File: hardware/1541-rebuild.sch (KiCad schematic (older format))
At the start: 9 parts, among them IC1 ATMEGA1284P-P, P1 CONN_01X02, X1 20Mhz

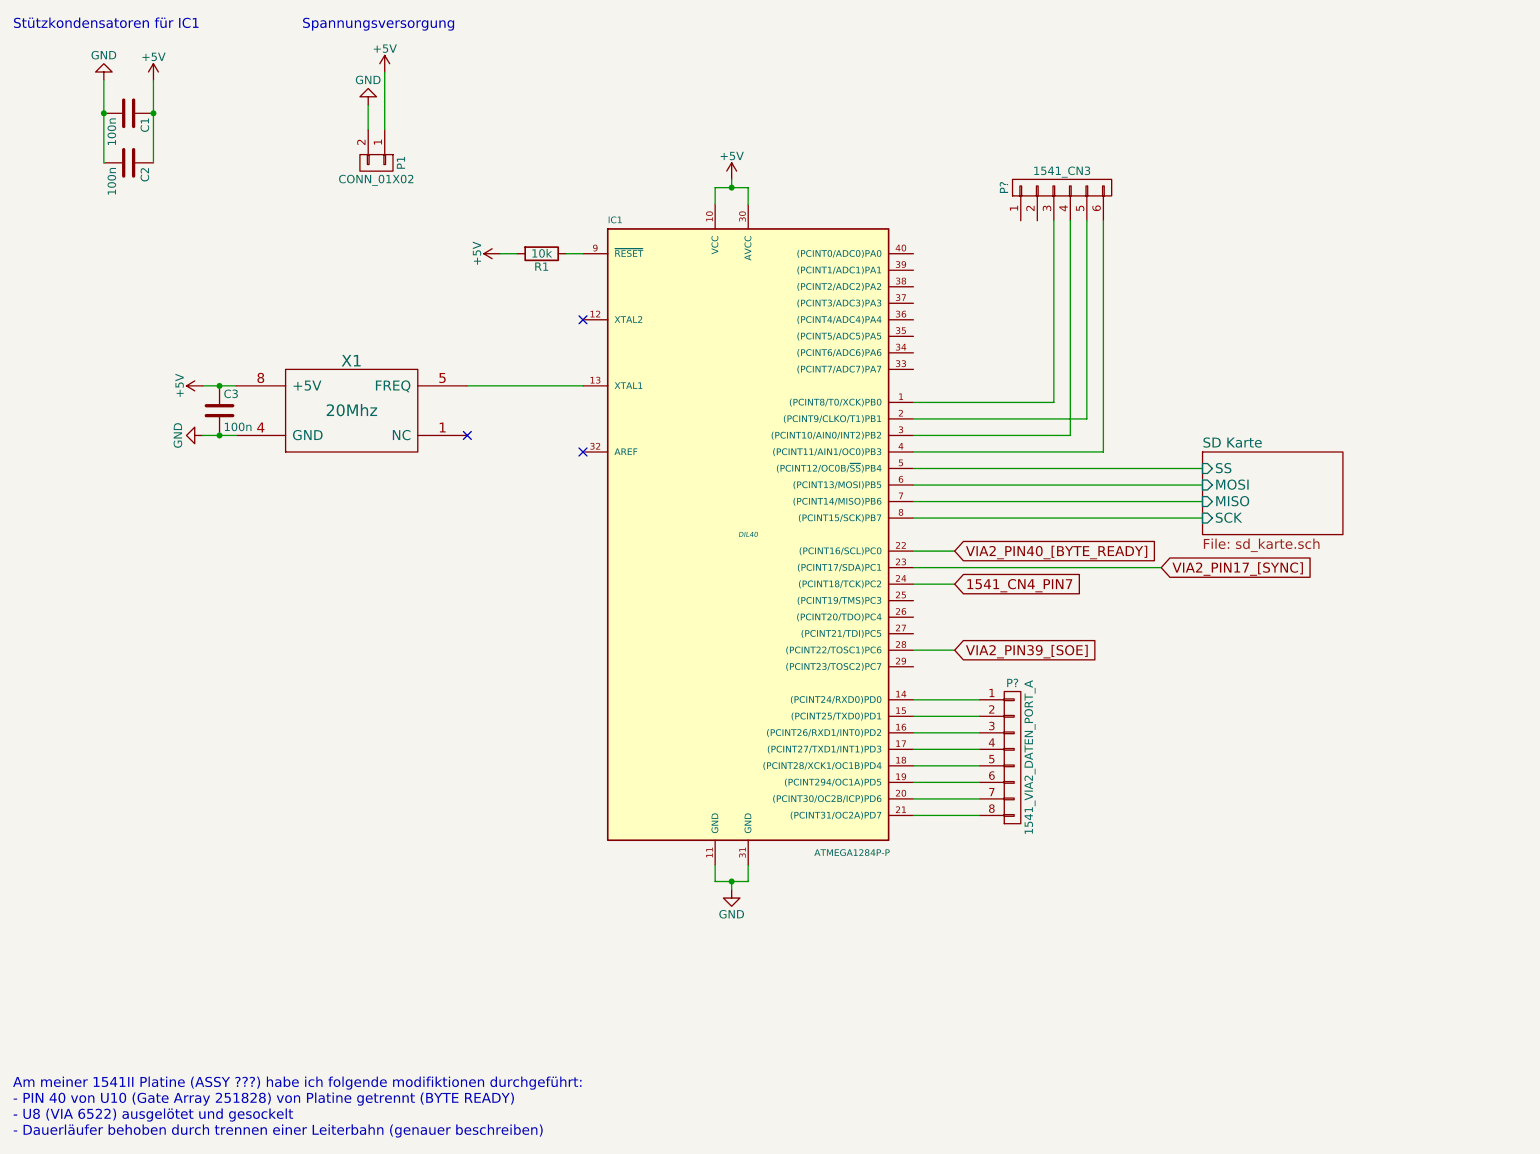
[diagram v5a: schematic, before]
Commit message: Schaltplan weiter entwickelt und Layout angefangen
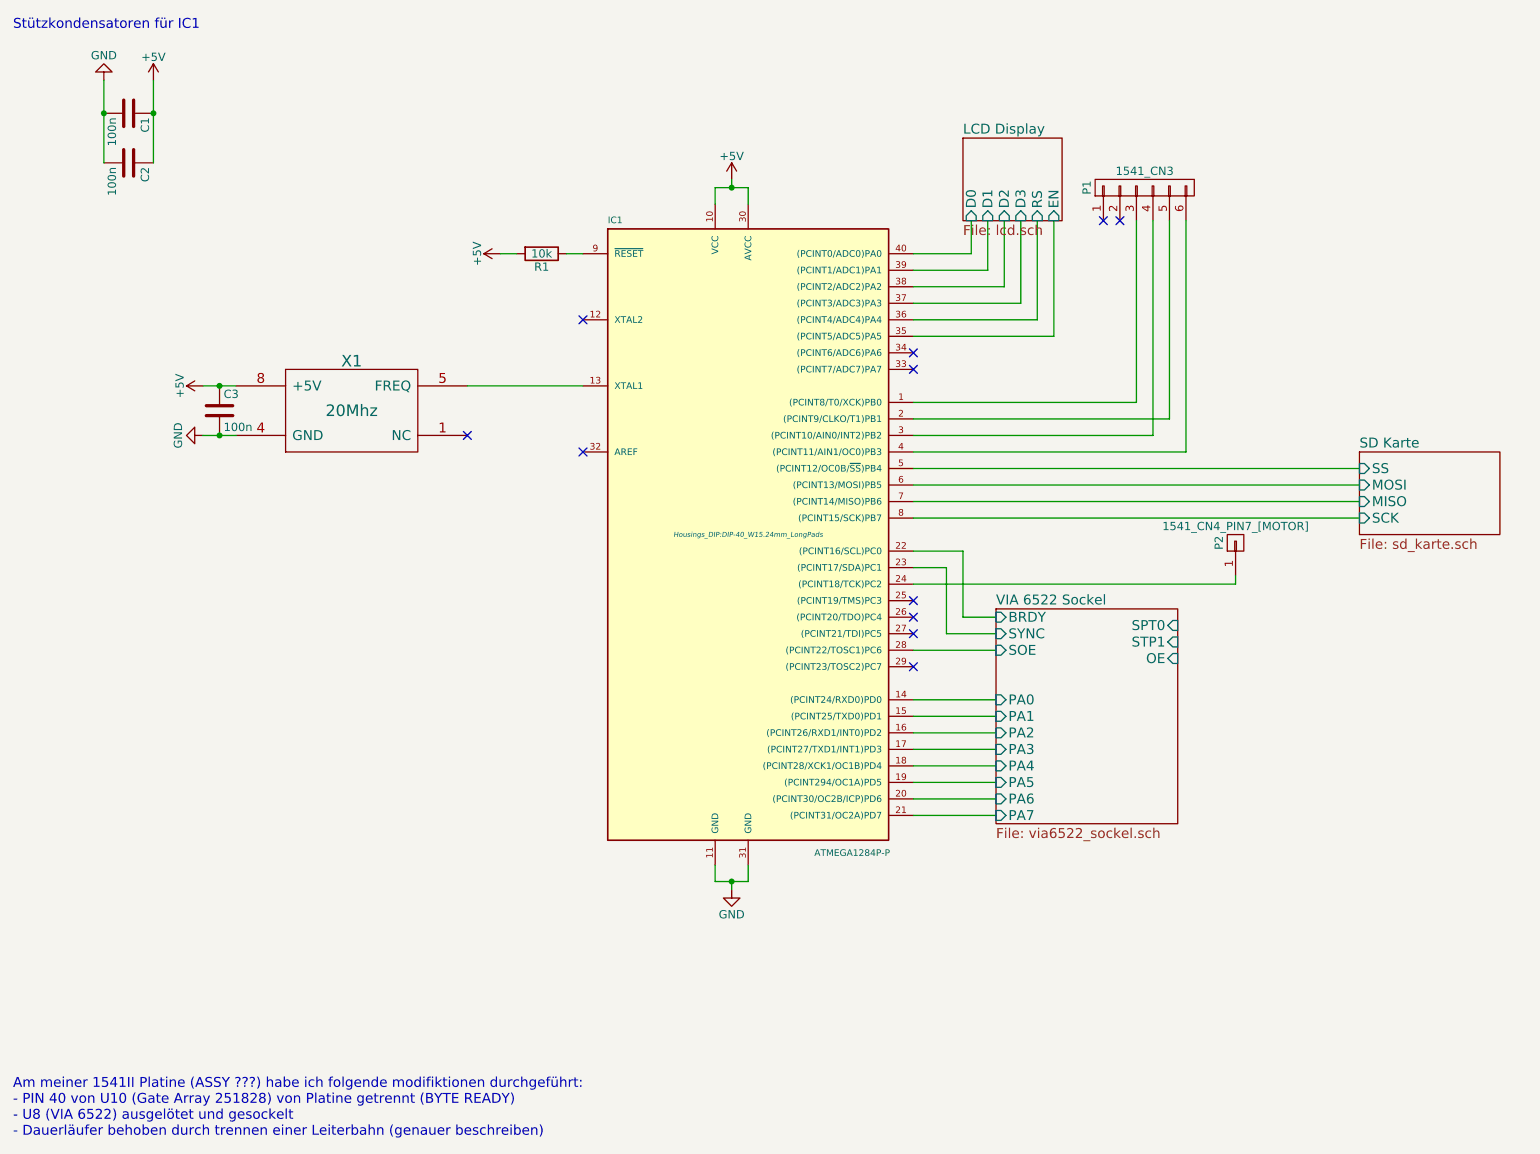
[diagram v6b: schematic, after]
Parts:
- removed P1: CONN_01X02, symbol CONN_01X02
- removed P?: 1541_VIA2_DATEN_PORT_A, symbol CONN_01X08
- added P2: 1541_CN4_PIN7_[MOTOR], Pin_Headers:Pin_Header_Straight_1x01, symbol CONN_01X01
- C1, C2, C3: footprint (none) -> Capacitors_ThroughHole:C_Disc_D6_P5
- IC1: footprint DIL40 -> Housings_DIP:DIP-40_W15.24mm_LongPads
- P1: renamed from P?; footprint (none) -> Socket_Strips:Socket_Strip_Straight_1x06
- R1: footprint (none) -> Resistors_ThroughHole:Resistor_Horizontal_RM10mm
- X1: footprint (none) -> Oscillator-Modules:OSCILLATOR_KXO-200_LargePads
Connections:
- net VIA 6522 Sockel/PA0: now reaches IC1.14 ((PCINT24/RXD0)PD0)
- net VIA 6522 Sockel/PA1: now reaches IC1.15 ((PCINT25/TXD0)PD1)
- net VIA 6522 Sockel/PA2: now reaches IC1.16 ((PCINT26/RXD1/INT0)PD2)
- net VIA 6522 Sockel/PA3: now reaches IC1.17 ((PCINT27/TXD1/INT1)PD3)
- net VIA 6522 Sockel/PA4: now reaches IC1.18 ((PCINT28/XCK1/OC1B)PD4)
- net VIA 6522 Sockel/PA5: now reaches IC1.19 ((PCINT294/OC1A)PD5)
- net VIA 6522 Sockel/PA6: now reaches IC1.20 ((PCINT30/OC2B/ICP)PD6)
- net VIA 6522 Sockel/PA7: now reaches IC1.21 ((PCINT31/OC2A)PD7)
- net LCD Display/EN: now reaches IC1.35 ((PCINT5/ADC5)PA5)
- net LCD Display/RS: now reaches IC1.36 ((PCINT4/ADC4)PA4)
- net LCD Display/D3: now reaches IC1.37 ((PCINT3/ADC3)PA3)
- net LCD Display/D2: now reaches IC1.38 ((PCINT2/ADC2)PA2)
- net LCD Display/D1: now reaches IC1.39 ((PCINT1/ADC1)PA1)
- net LCD Display/D0: now reaches IC1.40 ((PCINT0/ADC0)PA0)
- net 1541_CN4_PIN7: no longer names the net of IC1.24 ((PCINT18/TCK)PC2)
- net 1541_CN4_PIN7: now also P2.1 (P1)
- net VIA2_PIN17_[SYNC] renamed VIA 6522 Sockel/SYNC
- net VIA2_PIN39_[SOE] renamed VIA 6522 Sockel/SOE
- net VIA2_PIN40_[BYTE_READY] renamed VIA 6522 Sockel/BRDY
- no-connect marks 3 -> 11
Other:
- note removed: "Spannungsversorgung"
- moved on the sheet: P1
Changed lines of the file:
@@
 $Descr A4 11693 8268
 encoding utf-8
-Sheet 1 2
+Sheet 1 4
 Title "1541-rebuild"
 Date "2015-09-15"
@@
 F 0 "IC1" H 4250 5680 40  0000 L BNN
 F 1 "ATMEGA1284P-P" H 5500 1850 40  0000 L BNN
-F 2 "DIL40" H 5100 3800 30  0000 C CIN
+F 2 "Housings_DIP:DIP-40_W15.24mm_LongPads" H 5100 3800 30  0000 C CIN
 F 3 "" H 5100 3800 60  0000 C CNN
 	1    5100 3800
@@
 F 0 "X1" H 2700 3350 70  0000 C CNN
 F 1 "20Mhz" H 2700 3050 70  0000 C CNN
-F 2 "" H 2700 3050 60  0000 C CNN
+F 2 "Oscillator-Modules:OSCILLATOR_KXO-200_LargePads" H 2700 3050 60  0001 C CNN
 F 3 "" H 2700 3050 60  0000 C CNN
 	1    2700 3050
@@
 F 0 "C3" H 1925 3150 50  0000 L CNN
 F 1 "100n" H 1925 2950 50  0000 L CNN
-F 2 "" H 1938 2900 30  0000 C CNN
+F 2 "Capacitors_ThroughHole:C_Disc_D6_P5" H 1938 2900 30  0001 C CNN
 F 3 "" H 1900 3050 60  0000 C CNN
 	1    1900 3050
@@
 F 0 "R1" V 3930 2100 50  0000 C CNN
 F 1 "10k" V 3850 2100 50  0000 C CNN
-F 2 "" V 3780 2100 30  0000 C CNN
+F 2 "Resistors_ThroughHole:Resistor_Horizontal_RM10mm" V 3780 2100 30  0001 C CNN
 F 3 "" H 3850 2100 30  0000 C CNN
 	1    3850 2100
@@
 F 0 "C1" H 1375 1350 50  0000 L CNN
 F 1 "100n" H 1375 1150 50  0000 L CNN
-F 2 "" H 1388 1100 30  0000 C CNN
+F 2 "Capacitors_ThroughHole:C_Disc_D6_P5" H 1388 1100 30  0001 C CNN
 F 3 "" H 1350 1250 60  0000 C CNN
 	1    1350 1250
@@
 F 0 "C2" H 1375 1650 50  0000 L CNN
 F 1 "100n" H 1375 1450 50  0000 L CNN
-F 2 "" H 1388 1400 30  0000 C CNN
+F 2 "Capacitors_ThroughHole:C_Disc_D6_P5" H 1388 1400 30  0001 C CNN
 F 3 "" H 1350 1550 60  0000 C CNN
 	1    1350 1550
@@
 Stützkondensatoren für IC1
 Wire Wire Line
-	6100 3400 7850 3400
-Wire Wire Line
-	6100 3500 7850 3500
-Wire Wire Line
-	6100 3600 7850 3600
-Wire Wire Line
-	6100 3700 7850 3700
+	6100 3400 8800 3400
+Wire Wire Line
+	6100 3500 8800 3500
+Wire Wire Line
+	6100 3600 8800 3600
+Wire Wire Line
+	6100 3700 8800 3700
 $Sheet
-S 7850 3300 850  500
+S 8800 3300 850  500
 U 55F7A0F9
 F0 "SD Karte" 60
 F1 "sd_karte.sch" 60
-F2 "MISO" I L 7850 3600 60
-F3 "SCK" I L 7850 3700 60
-F4 "MOSI" I L 7850 3500 60
-F5 "SS" I L 7850 3400 60
+F2 "MISO" I L 8800 3600 60
+F3 "SCK" I L 8800 3700 60
+F4 "MOSI" I L 8800 3500 60
+F5 "SS" I L 8800 3400 60
 $EndSheet
 $Comp
-L CONN_01X02 P1
-U 1 1 55F8BDD8
-P 2850 1550
-F 0 "P1" H 2850 1700 50  0000 C CNN
-F 1 "CONN_01X02" V 2950 1550 50  0000 C CNN
-F 2 "" H 2850 1550 60  0000 C CNN
-F 3 "" H 2850 1550 60  0000 C CNN
-	1    2850 1550
-	0    1    1    0
-$EndComp
-Text Notes 2400 750  0    60   ~ 0
-Spannungsversorgung
-$Comp
-L GND #PWR08
-U 1 1 55F8C133
-P 2800 1200
-F 0 "#PWR08" H 2800 950 50  0001 C CNN
-F 1 "GND" H 2800 1050 50  0000 C CNN
-F 2 "" H 2800 1200 60  0000 C CNN
-F 3 "" H 2800 1200 60  0000 C CNN
-	1    2800 1200
-	-1   0    0    1
-$EndComp
-$Comp
-L +5V #PWR09
-U 1 1 55F8C16D
-P 2900 1000
-F 0 "#PWR09" H 2900 850 50  0001 C CNN
-F 1 "+5V" H 2900 1140 50  0000 C CNN
-F 2 "" H 2900 1000 60  0000 C CNN
-F 3 "" H 2900 1000 60  0000 C CNN
-	1    2900 1000
-	1    0    0    -1
-$EndComp
-Wire Wire Line
-	2900 1000 2900 1350
-Wire Wire Line
-	2800 1200 2800 1350
-$Comp
-L CONN_01X06 P?
+L CONN_01X06 P1
 U 1 1 55F8E45C
-P 7000 1700
-F 0 "P?" H 7000 2050 50  0000 C CNN
-F 1 "1541_CN3" V 7100 1700 50  0000 C CNN
-F 2 "" H 7000 1700 60  0000 C CNN
-F 3 "" H 7000 1700 60  0000 C CNN
-	1    7000 1700
+P 7500 1700
+F 0 "P1" H 7500 2050 50  0000 C CNN
+F 1 "1541_CN3" V 7600 1700 50  0000 C CNN
+F 2 "Socket_Strips:Socket_Strip_Straight_1x06" H 7500 1700 60  0001 C CNN
+F 3 "" H 7500 1700 60  0000 C CNN
+	1    7500 1700
 	0    -1   -1   0
 $EndComp
 Wire Wire Line
-	6950 1900 6950 3000
-Wire Wire Line
-	6950 3000 6100 3000
-$Comp
-L CONN_01X08 P?
-U 1 1 55F921A0
-P 6700 5150
-F 0 "P?" H 6700 5600 50  0000 C CNN
-F 1 "1541_VIA2_DATEN_PORT_A" V 6800 5150 50  0000 C CNN
-F 2 "" H 6700 5150 60  0000 C CNN
-F 3 "" H 6700 5150 60  0000 C CNN
-	1    6700 5150
-	1    0    0    -1
-$EndComp
-Wire Wire Line
-	6500 4800 6100 4800
-Wire Wire Line
-	6500 4900 6100 4900
-Wire Wire Line
-	6500 5000 6100 5000
-Wire Wire Line
-	6500 5100 6100 5100
-Wire Wire Line
-	6500 5200 6100 5200
-Wire Wire Line
-	6500 5300 6100 5300
-Wire Wire Line
-	6500 5400 6100 5400
-Wire Wire Line
-	6500 5500 6100 5500
-Text GLabel 6350 4100 2    60   Input ~ 0
-1541_CN4_PIN7
-Wire Wire Line
-	6100 4100 6350 4100
-Wire Wire Line
-	6100 3100 7150 3100
-Wire Wire Line
-	7150 3100 7150 1900
-Wire Wire Line
-	6100 3200 7050 3200
-Wire Wire Line
-	7050 3200 7050 1900
-Wire Wire Line
-	6100 3300 7250 3300
-Wire Wire Line
-	7250 3300 7250 1900
-Wire Wire Line
-	6100 3900 6350 3900
-Text GLabel 6350 3900 2    60   Input ~ 0
-VIA2_PIN40_[BYTE_READY]
-Wire Wire Line
-	6100 4000 7600 4000
-Text GLabel 7600 4000 2    60   Input ~ 0
-VIA2_PIN17_[SYNC]
-Wire Wire Line
-	6100 4500 6350 4500
-Text GLabel 6350 4500 2    60   Input ~ 0
-VIA2_PIN39_[SOE]
+	7450 1900 7450 3000
+Wire Wire Line
+	7450 3000 6100 3000
+Wire Wire Line
+	6100 3100 7650 3100
+Wire Wire Line
+	7650 3100 7650 1900
+Wire Wire Line
+	6100 3200 7550 3200
+Wire Wire Line
+	7550 3200 7550 1900
+Wire Wire Line
+	6100 3300 7750 3300
+Wire Wire Line
+	7750 3300 7750 1900
+$Sheet
+S 6400 1400 600  500
+U 55F9179B
+F0 "LCD Display" 60
+F1 "lcd.sch" 60
+F2 "D0" I B 6450 1900 60
+F3 "D1" I B 6550 1900 60
+F4 "D2" I B 6650 1900 60
+F5 "D3" I B 6750 1900 60
+F6 "RS" I B 6850 1900 60
+F7 "EN" I B 6950 1900 60
+$EndSheet
+Wire Wire Line
+	6450 1900 6450 2100
+Wire Wire Line
+	6450 2100 6100 2100
+Wire Wire Line
+	6550 1900 6550 2200
+Wire Wire Line
+	6550 2200 6100 2200
+Wire Wire Line
+	6650 1900 6650 2300
+Wire Wire Line
+	6650 2300 6100 2300
+Wire Wire Line
+	6750 1900 6750 2400
+Wire Wire Line
+	6750 2400 6100 2400
+Wire Wire Line
+	6850 1900 6850 2500
+Wire Wire Line
+	6850 2500 6100 2500
+Wire Wire Line
+	6950 1900 6950 2600
+Wire Wire Line
+	6950 2600 6100 2600
+NoConn ~ 7250 1900
+NoConn ~ 7350 1900
+NoConn ~ 6100 2700
+NoConn ~ 6100 2800
+NoConn ~ 6100 4200
+NoConn ~ 6100 4300
+NoConn ~ 6100 4400
+NoConn ~ 6100 4600
+$Sheet
+S 6600 4250 1100 1300
+U 55F9B22C
+F0 "VIA 6522 Sockel" 60
+F1 "via6522_sockel.sch" 60
+F2 "PA0" I L 6600 4800 60
+F3 "PA1" I L 6600 4900 60
+F4 "PA2" I L 6600 5000 60
+F5 "PA3" I L 6600 5100 60
+F6 "PA4" I L 6600 5200 60
+F7 "PA5" I L 6600 5300 60
+F8 "PA6" I L 6600 5400 60
+F9 "PA7" I L 6600 5500 60
+F10 "BRDY" I L 6600 4300 60
+F11 "SPT0" I R 7700 4350 60
+F12 "STP1" I R 7700 4450 60
+F13 "SYNC" I L 6600 4400 60
+F14 "OE" I R 7700 4550 60
+F15 "SOE" I L 6600 4500 60
+$EndSheet
+Wire Wire Line
+	6100 4800 6600 4800
+Wire Wire Line
+	6100 4900 6600 4900
+Wire Wire Line
+	6100 5000 6600 5000
+Wire Wire Line
+	6100 5100 6600 5100
+Wire Wire Line
+	6100 5200 6600 5200
+Wire Wire Line
+	6100 5300 6600 5300
+Wire Wire Line
+	6100 5400 6600 5400
+Wire Wire Line
+	6100 5500 6600 5500
+Wire Wire Line
+	6100 4500 6600 4500
+Wire Wire Line
+	6100 4000 6300 4000
+Wire Wire Line
+	6300 4000 6300 4400
+Wire Wire Line
+	6300 4400 6600 4400
+Wire Wire Line
+	6100 3900 6400 3900
+Wire Wire Line
+	6400 3900 6400 4300
+Wire Wire Line
+	6400 4300 6600 4300
+$Comp
+L CONN_01X01 P2
+U 1 1 55F9A2C7
+P 8050 3850
+F 0 "P2" H 8050 3950 50  0000 C CNN
+F 1 "1541_CN4_PIN7_[MOTOR]" V 8150 3850 50  0000 C CNN
+F 2 "Pin_Headers:Pin_Header_Straight_1x01" H 8050 3850 60  0001 C CNN
+F 3 "" H 8050 3850 60  0000 C CNN
+	1    8050 3850
+	0    -1   -1   0
+$EndComp
+Wire Wire Line
+	6100 4100 8050 4100
+Wire Wire Line
+	8050 4100 8050 4050
 $EndSCHEMATC
